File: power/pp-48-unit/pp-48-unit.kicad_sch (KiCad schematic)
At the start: 0 parts

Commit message: pp-48 chained plane: unit board 76 x 72 (9 mm left margin for chain IN J301 + holes, user; slots as rev1 at x 100 / 125; 17 mm input strip with XT60, unit hot-swap, chain OUT J302) and core board 56 x 72 (rev1 core minus the tile, 8 mm right margin for chain OUT J301 + holes, mux U6 by the header, XT30 at the bottom) placed as drafts by tools/place_unit.py / place_core.py (boardfit.py helpers); chain headers on B, pins at v 39..61 on every board; pinout swapped so IN pin 1 = 3V3 / P0 at the bottom on B (flat cable n -> 13 - n); DRC 0 errors besides unconnected, parity clean; not routed; handoff
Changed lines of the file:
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@@
 			)
 		)
-		(pin "SCL" bidirectional
+		(pin "SDA" bidirectional
 			(at 215.9 40.64 180)
 			(effects
@@
 			)
 		)
-		(pin "SDA" bidirectional
+		(pin "SCL" bidirectional
 			(at 215.9 43.18 180)
 			(effects
@@
 		)
 	)
-	(label "SEG_SCL"
+	(label "SEG_SDA"
 		(at 208.28 40.64 180)
 		(effects
@@
 		)
 	)
-	(label "SEG_SDA"
+	(label "SEG_SCL"
 		(at 208.28 43.18 180)
 		(effects

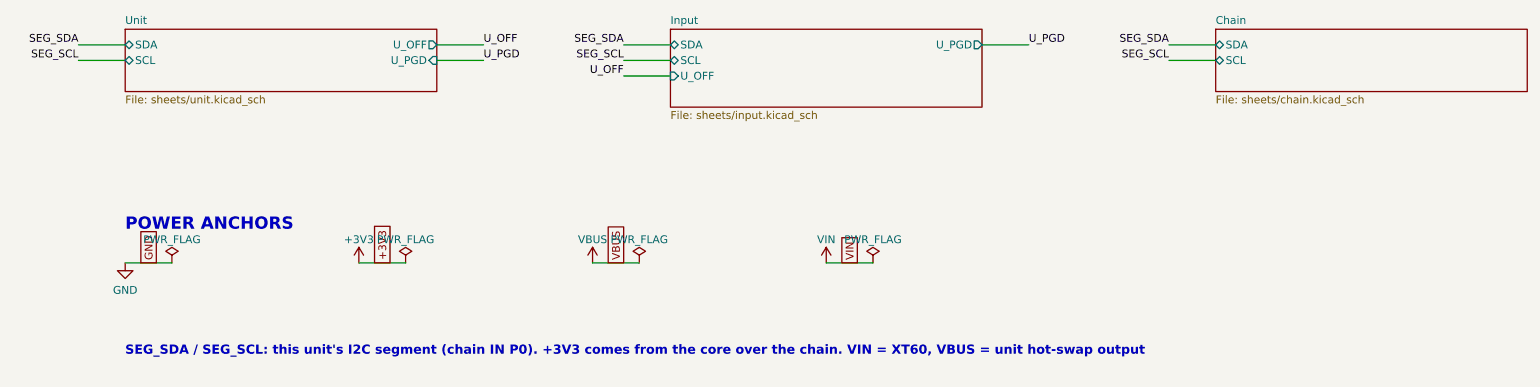
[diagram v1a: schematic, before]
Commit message: pp-48 plane boards: press deadline line (docs/press-deadline-line.md decided: option B + A) on a 14-pin chain (S14B-PH-K-S C157938; 13 PRESS_EN, 14 EXP_RSTN, cable n -> 15 - n, pins v 35..61); unit Q10 / R31 switch the photoMOS LED returns (PRESS_RTN), core U301 74LVC1G123 deadline (pp:74LVC1G123 single-unit copy) on PC6 PRESS_TRIG, PC7 EXP_RSTN to the units' /RESET; ERC 0 both; boards rebuilt and placed, unit 78.5 x 72 with the strip power path re-placed top-down; unit routing tools (route_unit.py hand copper + In2 band / +3V3 trunk, unitsplit.py, route_unit.sh flow): DRC 0 errors, ~10 unconnected at expander U5; core placed, not routed; pmmount.py restored from granite_controller; ADR 0005 decision 4; handoff
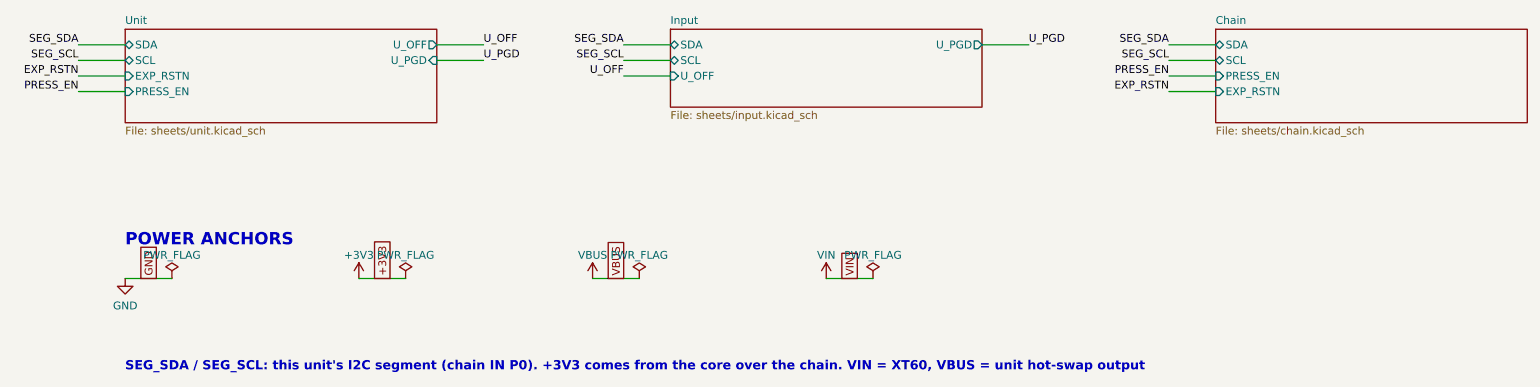
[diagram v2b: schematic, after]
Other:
- sheet Chain ports: added EXP_RSTN, PRESS_EN; removed none
- sheet Unit ports: added EXP_RSTN, PRESS_EN; removed none
